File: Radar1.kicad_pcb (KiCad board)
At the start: 4 copper layers, 66 x 46 mm, 99 parts, among them J1 USB4215-03-A, J2 Barrel_Jack, J3 SMA-2.92mm-EndLaunch, J4 SMA-2.92mm-EndLaunch, U1 BGT24LTR11N16, U10 93LC56B-I/SN, U11 445I23D12M00000, U12 AMM-8211PSM, U13 TPS7A4700RGWT, U14 TPS7A2033PDBVR, U15 TPD2E009DBZR, U16 REF5025AID, U2 ADF4159WCCPZ, U3 OPA1656ID, U4 TPS7A2033PDBVR, U5 TPS7A2018PDBVR, U6 TPS7A4700RGWT, U7 FT2232HL-REEL, U8 ADS8353IPW, U9 ADP5600ACPZ-R7, Y1 ECS-TXO-2520MV-500-AN-TR

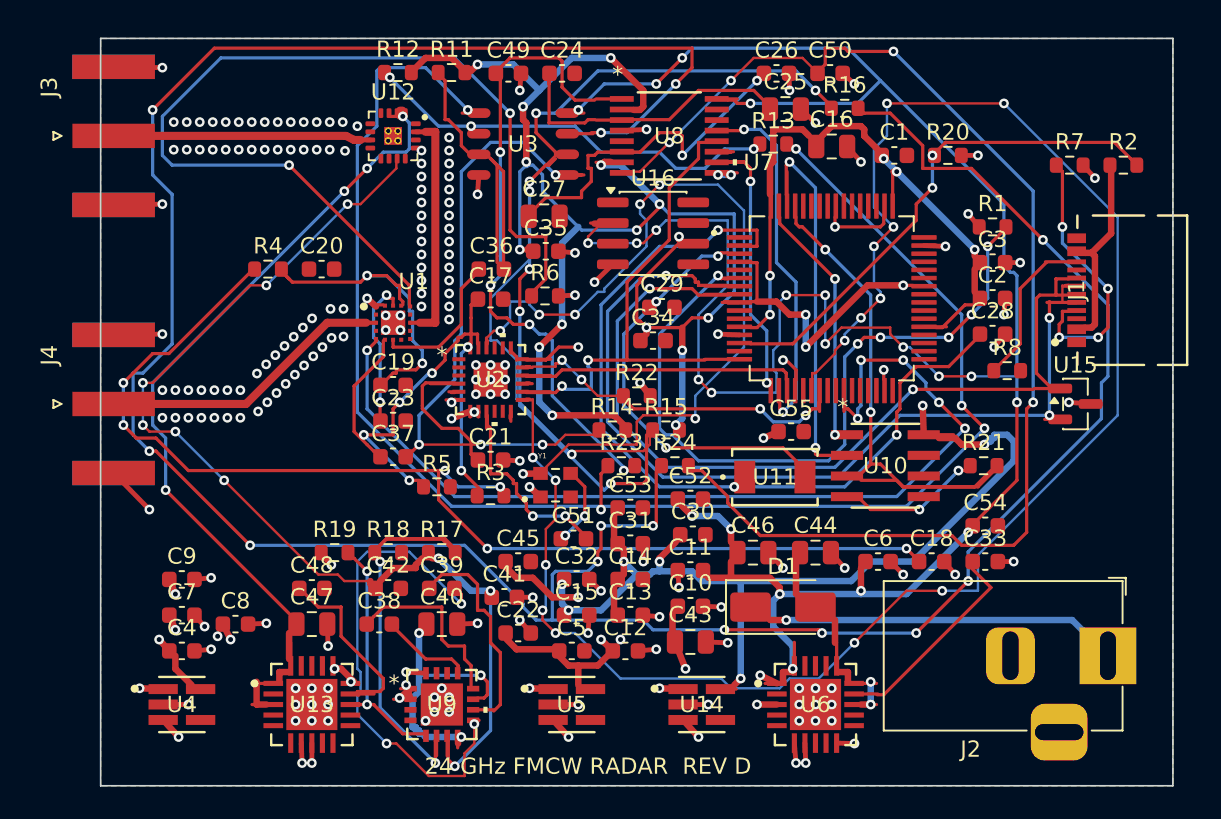
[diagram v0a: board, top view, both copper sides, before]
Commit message: Rev-E: PLL loop filter redesign — topology fix + computed values
The captured loop filter was an all-shunt RC ladder: a current-driven
ladder has no finite zero at V_TUNE, making the type-2 loop
unconditionally unstable (verified by exact network analysis, see
tools/pll_loop_filter.py). R4's input moves from the R3/C18 junction to
CPOUT, restoring the standard 3rd-order passive topology.

Values from BGT24LTR11 DS (Kvco 720M/2G Hz/V, VTUNE 0.7-2.5V, /16) and
ADF4159 (RSET 5.1k, Icp 2.5mA, fPFD 50MHz, N=483):
C17 910pF, R3 270R, C18 15nF, R4 560R, C19 270pF
-> fc 146 kHz, PM 52 deg (typ); all corners in docs/PLL-LOOP-FILTER.md.

Schematic: R4.1 global label LF_B->LF_A + 5 values (netlist regression:
exactly that delta). Board: R4.1 pad re-netted, LF_A/LF_B ripped and
rerouted, stale-geometry clearance/crossing defects from earlier heals
fixed (0 shorts / 0 clearance / 0 crossings). Routing backlog now 6 nets.

Co-Authored-By: Claude Fable 5 <noreply@anthropic.com>
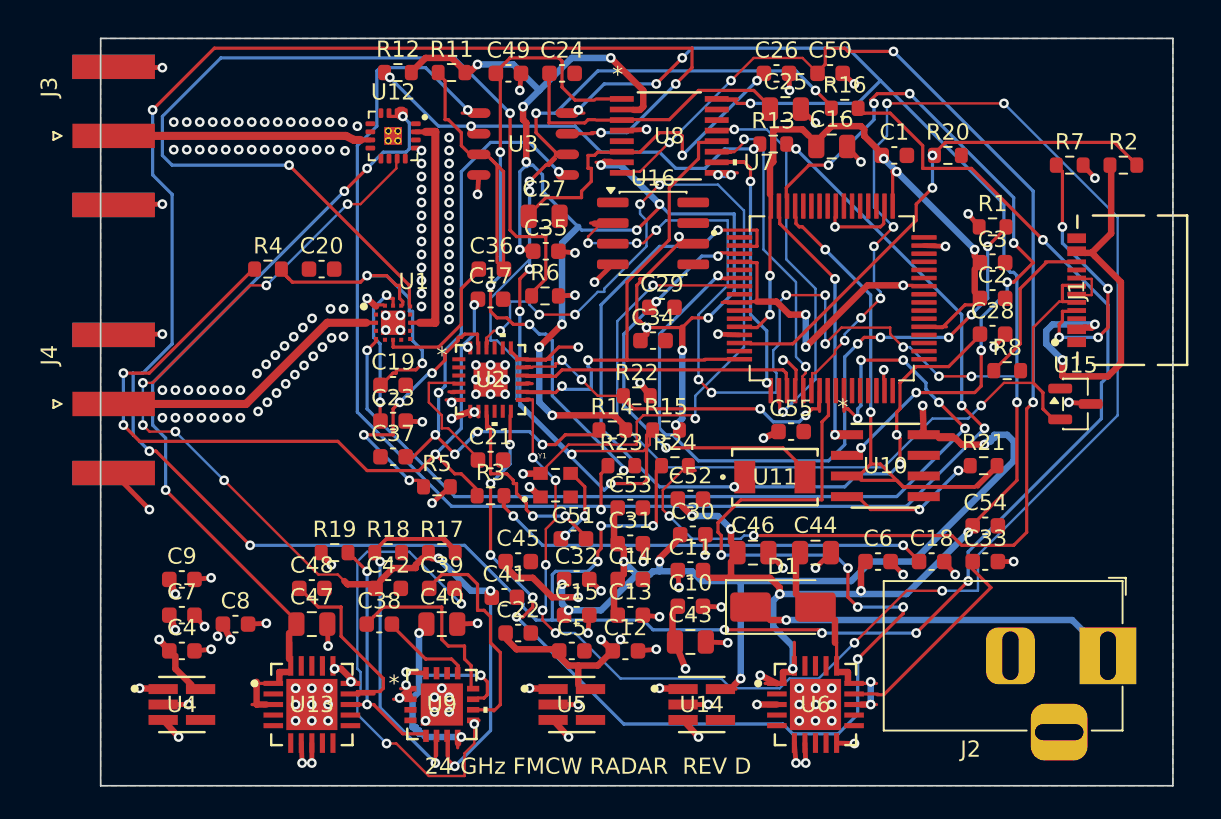
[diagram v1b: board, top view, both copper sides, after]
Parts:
- C17: value 1nF -> 910pF
- C18: value 10nF -> 15nF
- C19: value 470pF -> 270pF
- R3: value 10k -> 270R
- R4: value 2.2k -> 560R
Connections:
- R4 pad 1: LF_B -> LF_A
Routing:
- net ADF_TXDATA: track 0.81 -> 75.9 mm, vias 0 -> 10
- net USB_DP: track 56.0 -> 2.20 mm, vias 2 -> 0
- net LF_B: track 70.7 -> 27.7 mm, vias 6 -> 2
- net LF_A: track 12.1 -> 48.5 mm, vias 2 -> 5
- net EE_CLK: track 24.7 -> 43.7 mm, vias 2 -> 8
- net CS_ADC: track 1.23 -> 19.4 mm, vias 0 -> 2
- net VBUS: track 11.1 -> 24.4 mm, vias 0 -> 2
- net IFQ_IN: track 8.24 -> 0.00 mm
- net USB_DM: track 59.8 -> 53.3 mm, vias 3 -> 2
- net ADC_B: track 76.5 -> 80.4 mm, vias 4 -> 6
- net RFINB_N: track 10.1 -> 7.39 mm
- net GND: track 70.5 -> 68.3 mm, vias 181 -> 178
- net OSC_I: track 51.2 -> 52.6 mm, vias 3 -> 4
- net REFA_N: track 16.7 -> 17.7 mm
- net SPI_MISO: track 21.9 -> 22.8 mm
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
